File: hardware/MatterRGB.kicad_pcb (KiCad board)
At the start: 4 copper layers, 22 x 35 mm, 64 parts, among them J1 CDM806-04A-MP-F011-67, J2 USB4105, J3 CDM805-08A-FP-F011-67, Q1 2N7002KL3A-TP, SW1 NO, SW2 NO, U1 FUSB302B01MPX, U2 ESP32-S3-WROOM-1U-N8R8, U3 DRV8955, U4 ADA4098-2BCPZ-RL7, U5 LMR51610YFDBVR, U6 TPS7B4255DBVR

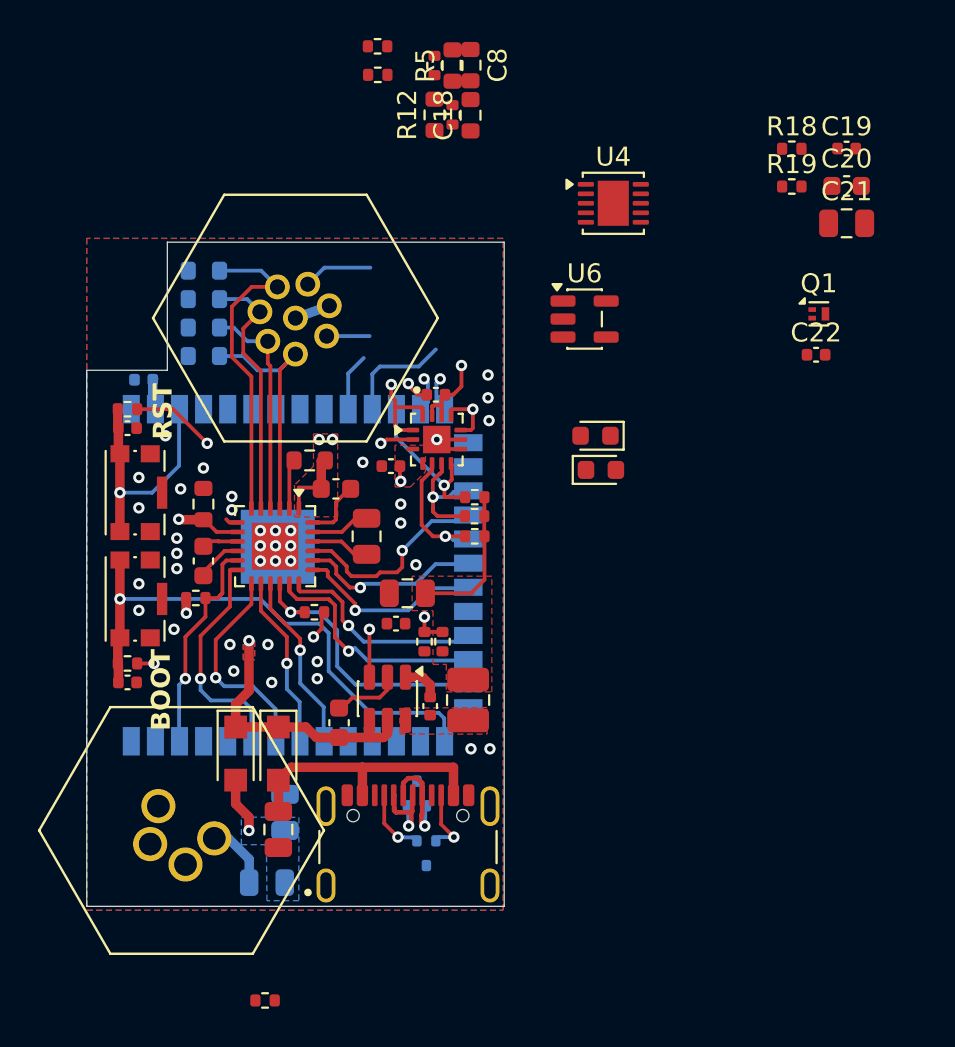
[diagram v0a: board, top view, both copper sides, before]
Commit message: Finished draft layout of muCM update.
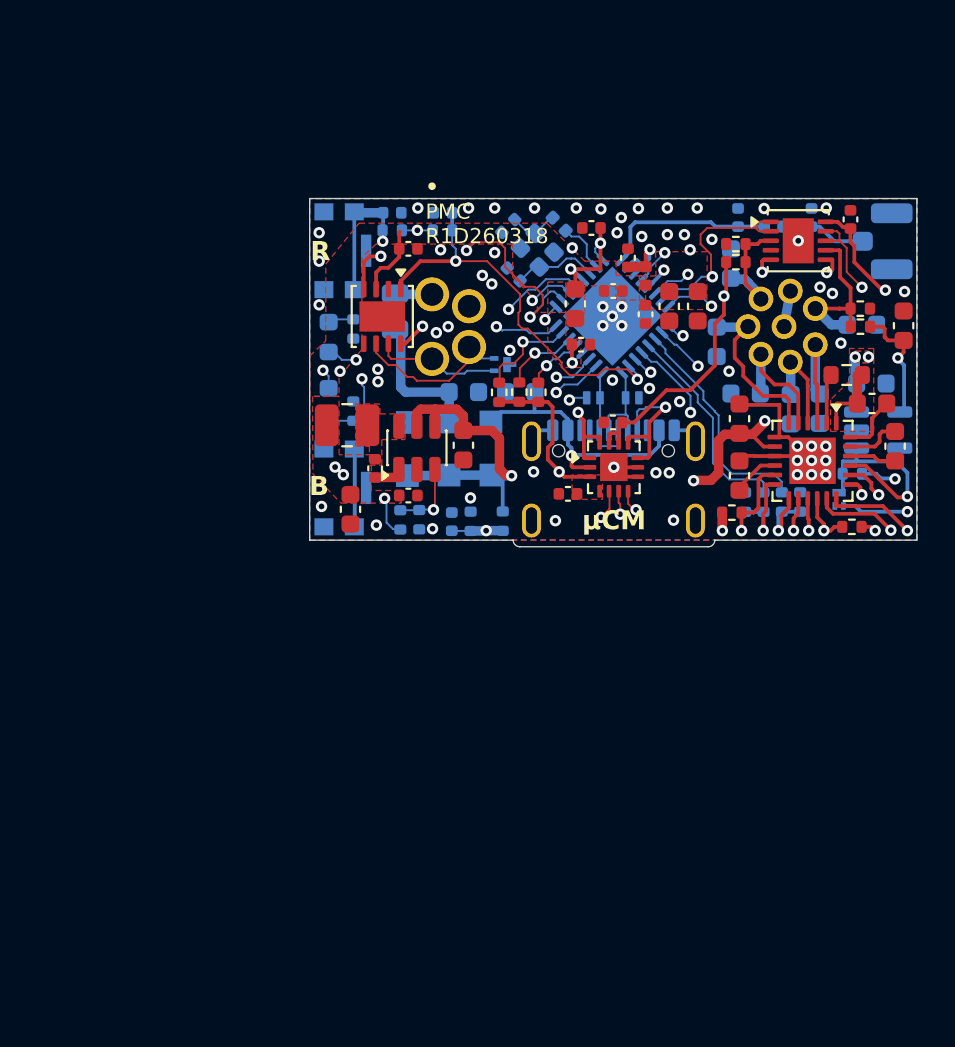
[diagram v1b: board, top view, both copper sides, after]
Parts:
- removed C15, C16: 5.6n, Capacitor_SMD:C_0402_1005Metric
- removed LED2: Red, LED_SMD:LED_0603_1608Metric
- removed R2: 2k, Resistor_SMD:R_0402_1005Metric
- removed R7, R8: 10k, Resistor_SMD:R_0402_1005Metric
- removed SW1, SW2: NO, Button_Switch_SMD:SW_Push_1P1T-SH_NO_CK_KMR2xxG
- added C23: 100nF, Capacitor_SMD:C_0603_1608Metric, F.Cu at (117.1, 90.7)
- added C24: 7pF, Capacitor_SMD:C_0402_1005Metric, B.Cu at (119.5, 79.1)
- added C25: 7pF, Capacitor_SMD:C_0402_1005Metric, B.Cu at (119.8, 81.7)
- added C26: 5.6n, Capacitor_SMD:C_0402_1005Metric, B.Cu at (113.3, 78.5)
- added C27: 5.6n, Capacitor_SMD:C_0402_1005Metric, B.Cu at (116.0, 78.5)
- added C32: 4pF, Capacitor_SMD:C_0402_1005Metric, B.Cu at (131.6, 78.7)
- added C33: 1u, Capacitor_SMD:C_0603_1608Metric, F.Cu at (123.0, 83.2)
- added C34: 1u, Capacitor_SMD:C_0603_1608Metric, F.Cu at (128.0, 83.4)
- added C36: 100n, Capacitor_SMD:C_0402_1005Metric, F.Cu at (125.0, 82.6)
- added C37: 100n, Capacitor_SMD:C_0402_1005Metric, F.Cu at (125.8, 80.8)
- added C38: 10 uF, Capacitor_SMD:C_0603_1608Metric, F.Cu at (129.4, 83.4)
- added C39: 100n, Capacitor_SMD:C_0402_1005Metric, F.Cu at (126.7, 83.8)
- added C40: 100n, Capacitor_SMD:C_0402_1005Metric, F.Cu at (123.3, 85.4)
- added C41: 10nF, Capacitor_SMD:C_0402_1005Metric, F.Cu at (123.8, 79.2)
- added D5: RCLAMP03391PW.C, Diode_SMD:D_SOD-882, B.Cu at (126.0, 88.2)
- added D6: RCLAMP03391PW.C, Diode_SMD:D_SOD-882, B.Cu at (124.0, 88.2)
- added J4: UF.L, Connector_Coaxial:U.FL_Hirose_U.FL-R-SMT-1_Vertical, B.Cu at (139.2, 80.0)
- added L1: 24 nH, Inductor_SMD:L_0402_1005Metric, B.Cu at (122.2, 79.0)
- added L3: 24 nH, Inductor_SMD:L_0402_1005Metric, B.Cu at (133.4, 79.2)
- added L4: 19R @ 100 MHz, Inductor_SMD:L_0402_1005Metric, F.Cu at (126.7, 81.8)
- added LED3: Red, LED_SMD:LED_0603_1608Metric, B.Cu at (110.0, 85.0)
- added Q2: 40 MHz, Crystal:Crystal_SMD_2016-4Pin_2.0x1.6mm, B.Cu at (121.0, 80.4)
- added R15: 10k, Resistor_SMD:R_0402_1005Metric, B.Cu at (113.3, 79.4)
- added R20: 10k, Resistor_SMD:R_0402_1005Metric, B.Cu at (116.0, 79.4)
- added R21: 2k, Resistor_SMD:R_0402_1005Metric, B.Cu at (111.3, 84.6)
- added R22: 10k, Resistor_SMD:R_0402_1005Metric, B.Cu at (133.9, 93.7)
- added R23: 4.75k, Resistor_SMD:R_0402_1005Metric, B.Cu at (134.8, 93.7)
- added R24: 10k, Resistor_SMD:R_0402_1005Metric, B.Cu at (132.9, 93.7)
- added R25: 4.75k, Resistor_SMD:R_0402_1005Metric, B.Cu at (131.9, 93.7)
- added SW3: NO, Button_Switch_SMD:SW_Push_1P1T-SH_NO_CK_KMR2xxG, B.Cu at (110.5, 80.5)
- added SW4: NO, Button_Switch_SMD:SW_Push_1P1T-SH_NO_CK_KMR2xxG, B.Cu at (110.5, 93.0)
- added U7: ESP32-C6, Package_DFN_QFN:QFN-32-1EP_5x5mm_P0.5mm_EP3.7x3.7mm, B.Cu at (125.0, 83.9)
- C1: footprint Capacitor_SMD:C_0805_2012Metric -> Capacitor_SMD:C_0603_1608Metric
- C10, C11, C12, C9: value 10 nF -> 47nF; footprint Resistor_SMD:R_0603_1608Metric -> Capacitor_SMD:C_0603_1608Metric
- C13: moved to F.Cu
- C14: value 10 nF -> 10nF; footprint Resistor_SMD:R_0603_1608Metric -> Capacitor_SMD:C_0603_1608Metric
- C18, C8: value 10 nF -> 10nF; footprint Resistor_SMD:R_0603_1608Metric -> Capacitor_SMD:C_0603_1608Metric; moved to B.Cu
- C19, D2, D3, J2, LED1, Q1, R14, R16, R17, R18, R19, R3, U6: moved to B.Cu
- C21, C3: value 100n -> 100nF; footprint Capacitor_SMD:C_0805_2012Metric -> Capacitor_SMD:C_0603_1608Metric; moved to B.Cu
- C29: value 10uF -> 10 uF; footprint Capacitor_SMD:C_0805_2012Metric -> Capacitor_SMD:C_0603_1608Metric
- C31: value 220nF -> 4pF; footprint Capacitor_SMD:C_0603_1608Metric -> Capacitor_SMD:C_0402_1005Metric; moved to B.Cu
- C5: value 100n -> 100nF; footprint Capacitor_SMD:C_0805_2012Metric -> Capacitor_SMD:C_0603_1608Metric
- D1: value RCLAMP0582B.TCT -> ESDCAN03; footprint Package_TO_SOT_SMD:SOT-416 -> PCM_PartyWagon112_DFN:DFN1006-3
- D4: value RCLAMP0582B.TCT -> PTVS40VS1UR,115; footprint Package_TO_SOT_SMD:SOT-416 -> Diode_SMD:Nexperia_CFP3_SOD-123W
- R12, R5: value 2.2kR -> 10k; footprint Resistor_SMD:R_0603_1608Metric -> Resistor_SMD:R_0402_1005Metric
- U2: value ESP32-S3-WROOM-1U-N8R8 -> TCAN3413DRBR; footprint RF_Module:ESP32-S3-WROOM-1U -> Package_SON:VSON-8-1EP_3x3mm_P0.65mm_EP1.6x2.4mm; moved to F.Cu
- moved R14 41.6 mm to (137.6, 92.2), turned to 180 degrees
- moved C31 36.5 mm to (135.4, 78.7)
- moved C10 32.7 mm to (135.9, 88.8), turned to -90 degrees
- moved C9 31.1 mm to (134.3, 88.8), turned to -90 degrees
- moved F1 30.8 mm to (113.5, 83.7), turned to 90 degrees
- moved J1 29.9 mm to (116.0, 84.5), turned to -90 degrees
- moved C11 29.3 mm to (132.0, 88.0)
- moved R4 28.7 mm to (137.6, 95.0)
- moved U3 28.7 mm to (135.5, 91.5)
- moved C7 28.7 mm to (137.3, 87.0)
- moved C19 28.6 mm to (116.5, 94.7), turned to 90 degrees
- moved C14 28.6 mm to (131.7, 89.3)
- moved C4 28.6 mm to (131.7, 92.3)
- moved R1 28.6 mm to (131.2, 94.2)
- moved C2 28.6 mm to (138.6, 88.5)
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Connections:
- net /VBAT_MEAS renamed /VMEAS_IN
- C10 pad 1: /OUT2 -> /OUT1
- C11 pad 1: /OUT3 -> /OUT4
- C12 pad 1: /OUT4 -> /OUT3
- C13 pad 1: +3V3 -> GND
- C13 pad 2: GND -> +3V3
- C17 pad 1: +3V3 -> +3.3VP
- C18 pad 1: /inputs/IN1 -> /IN1
- C20 pad 1: Net-(U6-OUT) -> +3.3VP
- C31 pad 1: VDC -> /MCU/ANT_
- C8 pad 1: /inputs/IN0 -> /IN0
- C9 pad 1: /OUT1 -> /OUT2
- D1 pad 1: USB_D+ -> /CAN+
- D1 pad 2: USB_D- -> /CAN-
- D4 pad 1: /CC1 -> VDC
- D4 pad 2: /CC2 -> GND
- J1 pad 3: unconnected-(J1-Pin_3-Pad3) -> /CAN+
- J1 pad 4: unconnected-(J1-Pin_4-Pad4) -> /CAN-
- Q1 pad 1: /inputs/SLEEP -> /SLEEP
- Q1 pad 3: Net-(Q1-D) -> /~{SLEEP}
- R12 pad 1: Net-(U6-OUT) -> +3.3VP
- R12 pad 2: /inputs/IN1 -> /IN0
- R13 pad 2: /inputs/IN1 -> /IN1
- R14 pad 2: Net-(Q1-D) -> /~{SLEEP}
- R5 pad 1: Net-(U6-OUT) -> +3.3VP
- R5 pad 2: /inputs/IN0 -> /IN1
- R6 pad 2: /inputs/IN0 -> /IN0
- U1 pad 12: +3V3 -> +3.3VP
- U1 pad 13: +3V3 -> +3.3VP
- U2 pad 1: GND -> /MCU/BOOT/CANTX
- U2 pad 2: +3V3 -> GND
- U2 pad 3: /RESET -> +3V3
- U2 pad 4: unconnected-(U2-IO4-Pad4) -> /MCU/CANRX
- U2 pad 5: unconnected-(U2-IO5-Pad5) -> +3V3
- U2 pad 6: unconnected-(U2-IO6-Pad6) -> /CAN-
- U2 pad 7: unconnected-(U2-IO7-Pad7) -> /CAN+
- U2 pad 8: /LED0 -> /SLEEP
- U2 pad 9: unconnected-(U2-IO16-Pad9) -> (no net)
- U3 pad 12: /VREF12/EN4 -> Net-(U3-VREF34/EN4)
- U3 pad 13: /VREF12/EN3 -> Net-(U3-VREF12/EN3)
- U4 pad 1: /inputs/IN1_MCU -> /IN0_MCU
- U4 pad 2: /inputs/IN1_MCU -> /IN0_MCU
- U4 pad 3: /inputs/IN1 -> /IN0
- U4 pad 5: /inputs/SLEEP -> /SLEEP
- U4 pad 6: /inputs/SLEEP -> /SLEEP
- U4 pad 7: /inputs/IN0 -> /IN1
- U4 pad 8: /inputs/IN0_MCU -> /IN1_MCU
- U4 pad 9: /inputs/IN0_MCU -> /IN1_MCU
- U6 pad 1: Net-(Q1-D) -> /~{SLEEP}
- U6 pad 4: Net-(U6-OUT) -> +3.3VP
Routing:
- net /SLEEP: track 0.00 -> 59.5 mm, vias 0 -> 5
- net /VMEAS_IN: track 0.00 -> 42.4 mm, vias 0 -> 2
- net /MCU/BOOT/CANTX: track 0.00 -> 38.8 mm, vias 0 -> 3
- net +3.3VP: track 0.00 -> 35.1 mm, vias 0 -> 2
- net /CC2: track 39.0 -> 5.02 mm, vias 2 -> 1
- net /BOOT: track 28.6 -> 0.00 mm, vias 1 -> 0
- net +3V3: track 59.1 -> 87.4 mm, vias 6 -> 14
- net USB_D-: track 31.8 -> 4.89 mm, vias 2 -> 0
- net USB_D+: track 32.6 -> 5.74 mm, vias 2 -> 0
- net /MCU/~{RST}: track 0.00 -> 25.4 mm, vias 0 -> 2
- net /CC1: track 32.7 -> 7.64 mm, vias 2 -> 1
- net VBUS: track 39.4 -> 14.7 mm
- net /OUT4_CPU: track 12.4 -> 36.1 mm, vias 1 -> 2
- net /OUT1_CPU: track 9.50 -> 29.9 mm, vias 1 -> 2
- net /MCU/LED0: track 0.00 -> 17.7 mm, vias 0 -> 2
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- removed copper zone on B.Cu, net /VDC_F
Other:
- board size 22 x 35 mm -> 32 x 18.3 mm
- board text added: "B"
- board text added: "PMC R1D260318"
- board text added: "R"
- board text added: "μCM"
- board text removed: "BOOT"
- board text removed: "Matter Controller"
- board text removed: "PMC R1D260211"
- board text removed: "RST"

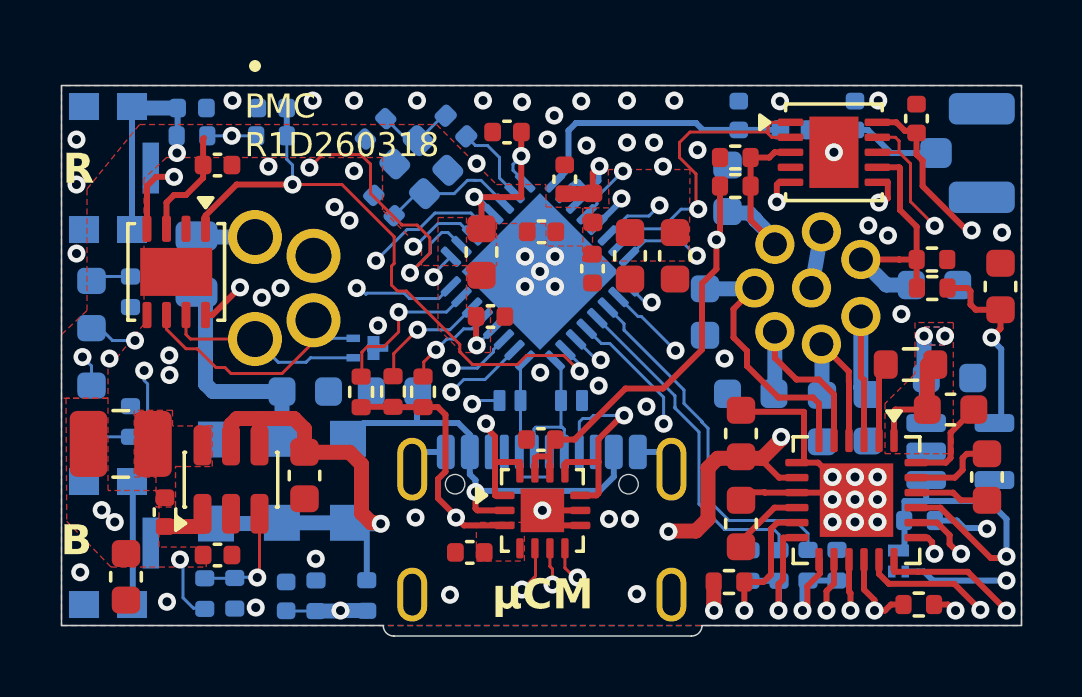
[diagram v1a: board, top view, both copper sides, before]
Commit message: removed backups
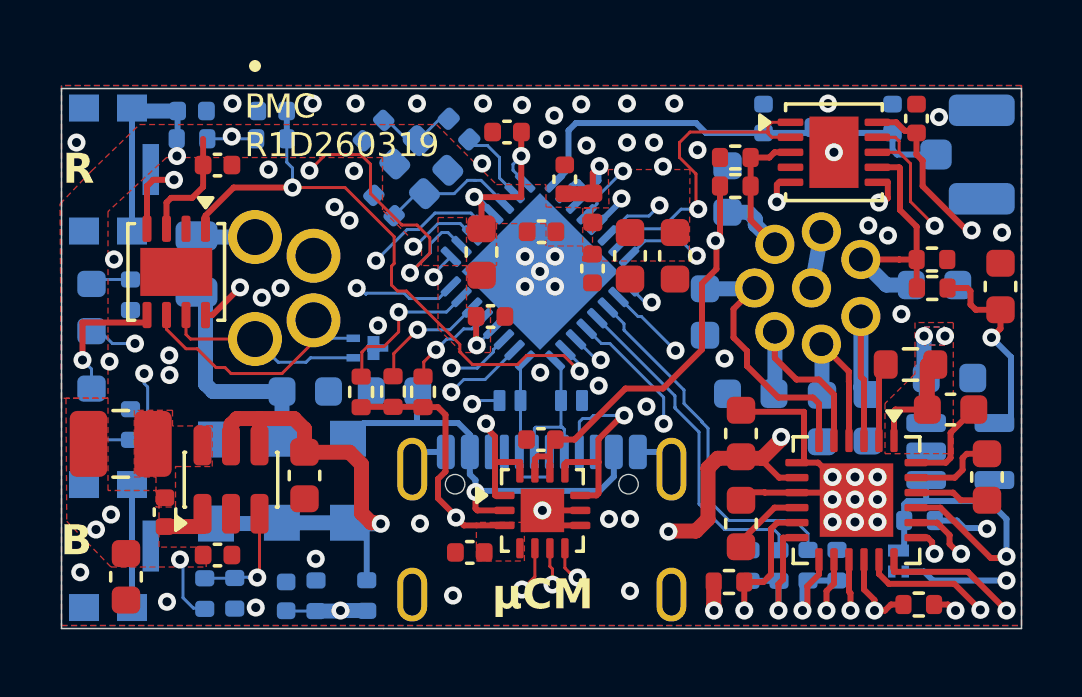
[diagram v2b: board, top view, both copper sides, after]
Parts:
- F1: value 5A -> 3A
- L2: value 6.8 uH -> 10uH
- R16: value 4.75k -> 31.6kR
- R17: value 4.75k -> 10k
- R18: value 4.75k -> 2k
- R19: value 10k -> 31.6kR
- moved C31 1.25 mm to (136.7, 78.8)
- moved L3 1.10 mm to (134.6, 79.1)
- moved C32 0.83 mm to (132.4, 78.8)
- moved L1 0.14 mm to (122.2, 79.2)
- moved LED1 0.10 mm to (110.0, 88.6)
- moved C26 0.10 mm to (113.3, 78.5)
- moved C27 0.10 mm to (116.0, 78.5)
- moved LED3 0.10 mm to (110.0, 85.1)
- moved R15 0.10 mm to (113.3, 79.5)
- moved R20 0.10 mm to (116.0, 79.5)
- moved R21 0.10 mm to (111.3, 84.7)
- moved R3 0.10 mm to (111.3, 89.0)
- moved SW4 0.10 mm to (110.5, 93.0)
- moved C24 0.09 mm to (119.4, 79.2)
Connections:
- U2 pad 9: (no net) -> GND
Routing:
- net +3V3: track 87.4 -> 90.9 mm
- net /VMEAS_IN: track 42.4 -> 43.8 mm
- net /MCU/ANT: track 9.18 -> 10.4 mm
- net /MCU/ANT_: track 4.54 -> 3.82 mm
- net +3.3VP: track 35.1 -> 35.7 mm
- net GND: vias 66 -> 65
- added copper zone on In1.Cu, net +3V3
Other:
- board size 32 x 18.3 mm -> 32 x 18 mm
- board text added: "PMC R1D260319"
- board text removed: "PMC R1D260318"
